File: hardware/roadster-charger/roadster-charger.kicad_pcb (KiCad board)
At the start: 4 copper layers, 74.4 x 50.2 mm, 98 parts, among them J1 USB4505-03-0-A, J2 USB4505-03-0-A, J3 54-00166, Q1 CSD19532Q5B, Q2 CSD19532Q5B, Q3 CSD19532Q5B, U1 MPM3606AGQV-P, U10 DAC70501ZDQFT, U11 LTC3786EUD#TRPBF, U2 ESP32-C3-MINI-1, U3 INA168, U4 OPA340NA, U5 FUSB307BMPX, U6 LM75B, U7 LM5050-1, U8 INA168, U9 OPA340NA

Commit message: change vout voltage divider to target max 2.5V @ 50V at battery
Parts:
- R18: value 15K -> 19.1K
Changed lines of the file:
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@@
     (descr "Resistor SMD 0603 (1608 Metric), square (rectangular) end terminal, IPC_7351 nominal, (Body size source: IPC-SM-782 page 72, https://www.pcb-3d.com/wordpress/wp-content/uploads/ipc-sm-782a_amendment_1_and_2.pdf), generated with kicad-footprint-generator")
     (tags "resistor")
-    (property "MPN" "RC0603JR-0715KL")
+    (property "MPN" "RMCF0603FT19K1")
     (property "Sheetfile" "roadster-charger.kicad_sch")
     (property "Sheetname" "")
@@
         (effects (font (size 1 1) (thickness 0.15)))
     )
-    (fp_text value "15K" (at 0 1.43 90) (layer "F.Fab") hide
+    (fp_text value "19.1K" (at 0 1.43 90) (layer "F.Fab") hide
         (effects (font (size 1 1) (thickness 0.15)))
     )

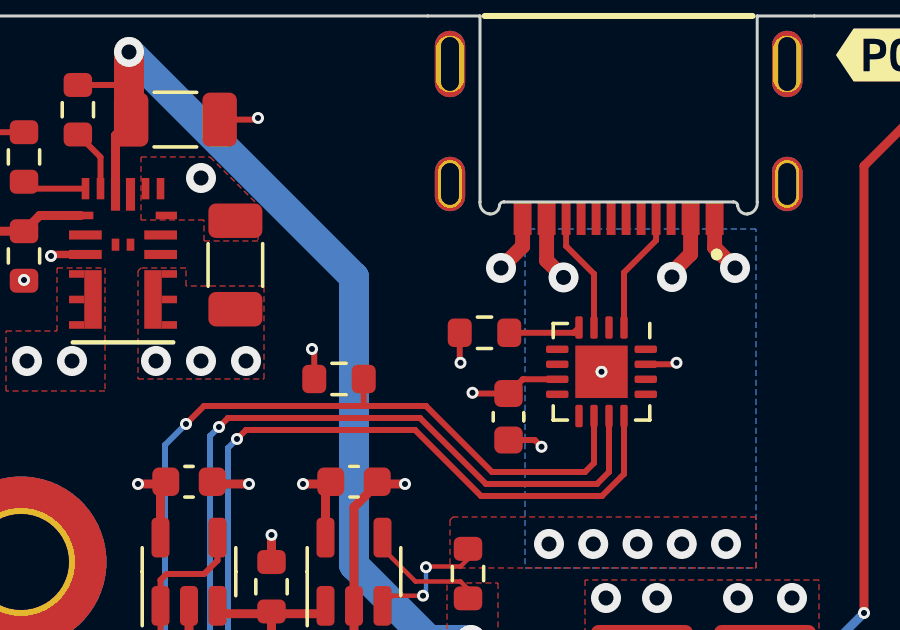
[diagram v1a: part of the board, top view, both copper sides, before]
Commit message: connect FUSB307 vbus pin
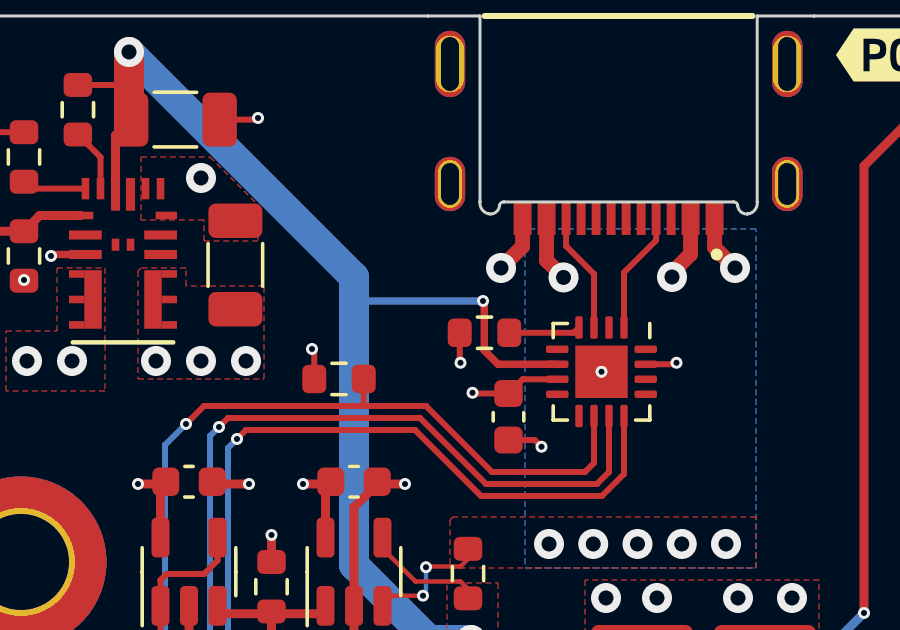
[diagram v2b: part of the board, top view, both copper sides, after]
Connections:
- U5 pad 6: unconnected-(U5-VBUS-Pad6) -> VBUS
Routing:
- net VBUS: track 62.2 -> 70.8 mm, vias 5 -> 6

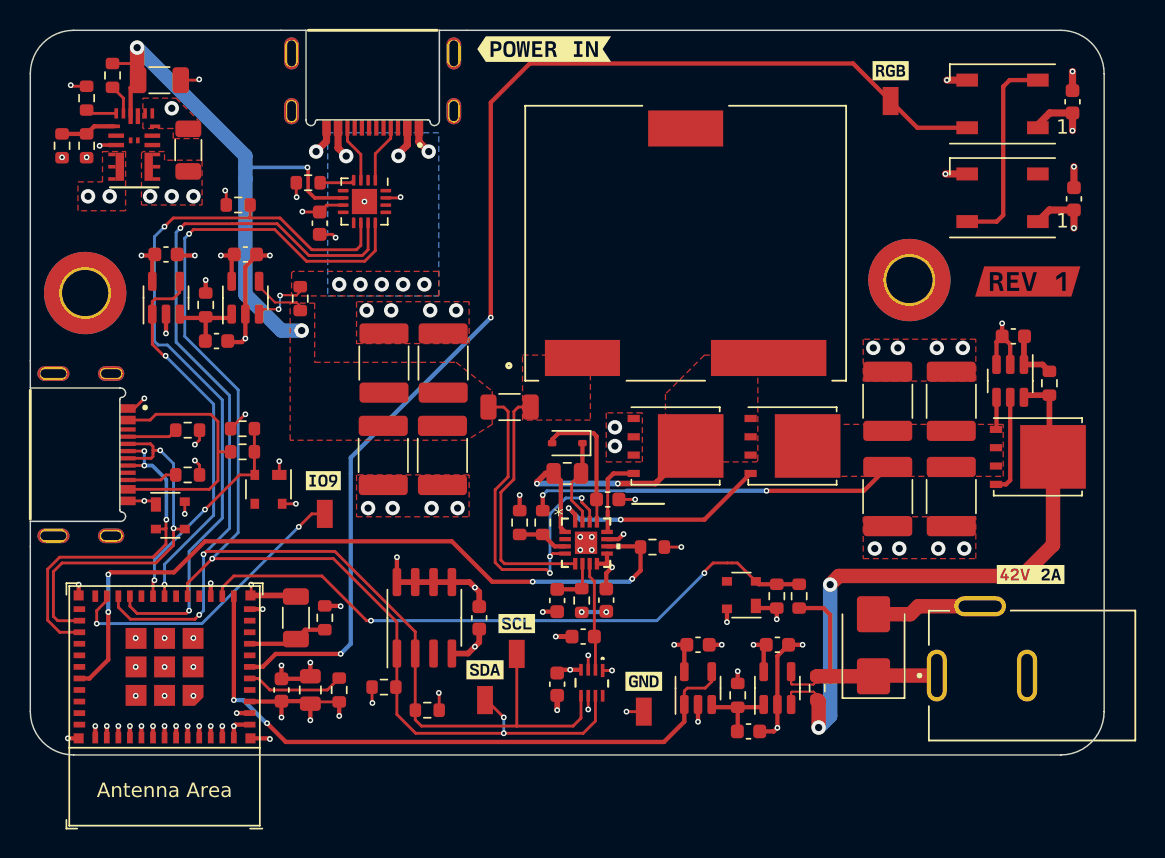
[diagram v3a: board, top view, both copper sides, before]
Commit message: Rough rev 2 layout
Move boost run pin to GPIO6 to avoid hard coded UART output
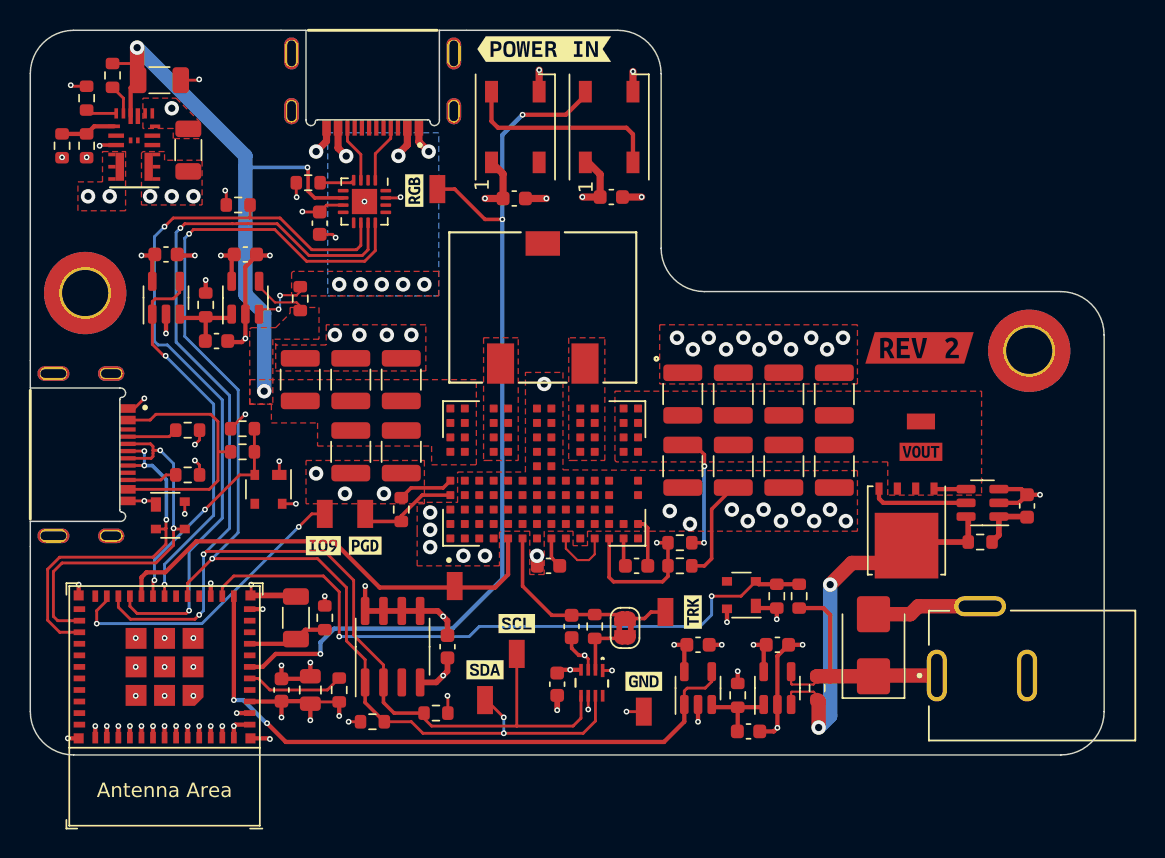
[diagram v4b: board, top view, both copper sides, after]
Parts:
- removed D7: D_Schottky_Small, Diode_SMD:D_SOD-323
- removed Q2, Q3: CSD19532Q5B, Package_TO_SOT_SMD:TDSON-8-1
- removed R22: 8.66K, Resistor_SMD:R_0603_1608Metric
- removed U11: LTC3786EUD#TRPBF, LTC3786EUD_TRPBF:QFN-16_UD
- removed kibuzzard-657BAFE4: G***, kibuzzard-657BAFE4
- removed kibuzzard-657BC539: G***, kibuzzard-657BC539
- removed kibuzzard-6581F29A: G***, kibuzzard-6581F29A
- removed kibuzzard-6581F2BF: G***, kibuzzard-6581F2BF
- added C31: 2.2uF, Capacitor_SMD:C_1210_3225Metric, F.Cu at (238.0, 139.5)
- added C32: 2.2uF, Capacitor_SMD:C_1210_3225Metric, F.Cu at (238.0, 134.5)
- added C33: 2.2uF, Capacitor_SMD:C_1210_3225Metric, F.Cu at (234.5, 134.5)
- added JP1: SolderJumper_2_Bridged, Jumper:SolderJumper-2_P1.3mm_Bridged2Bar_RoundedPad1.0x1.5mm, F.Cu at (223.5, 150.7)
- added TP6: RCU-0C, RCU-0C:TP+195X110, F.Cu at (205.5, 142.8)
- added TP7: RCU-0C, RCU-0C:TP+195X110, F.Cu at (211.7, 147.8)
- added TP8: RCU-0C, RCU-0C:TP+195X110, F.Cu at (226.3, 149.6)
- added TP9: RCU-0C, RCU-0C:TP+195X110, F.Cu at (244.0, 136.4)
- added U12: PI3740-00-LGIZ, PI3740-00-LGIZ:LGA108S100P10X14_1000X1400X263N, F.Cu at (217.9, 140.0)
- added kibuzzard-671EA982: G***, kibuzzard-671EA982, F.Cu at (205.5, 145.0)
- added kibuzzard-671EA992: G***, kibuzzard-671EA992, F.Cu at (228.2, 149.6)
- added kibuzzard-671EAE84: G***, kibuzzard-671EAE84, F.Cu at (208.9, 120.4)
- added kibuzzard-671EB1B0: G***, kibuzzard-671EB1B0, F.Cu at (243.9, 131.3)
- added kibuzzard-671EB361: G***, kibuzzard-671EB361, F.Cu at (244.0, 138.5)
- C19: value 15nF -> 56pF
- C20: value 220pF -> 4.7nF
- C21: value 0.1uF -> 2.2uF; footprint Capacitor_SMD:C_0805_2012Metric -> Capacitor_SMD:C_1210_3225Metric
- C22: value 4.7uF -> 2.2uF; footprint Capacitor_SMD:C_0603_1608Metric -> Capacitor_SMD:C_1210_3225Metric
- C23, C24, C25, C26, C27, C28, C29, C30: value 6.8uF -> 2.2uF; footprint Capacitor_SMD:C_1812_4532Metric -> Capacitor_SMD:C_1210_3225Metric
- L1: value 16uH -> PA5119.421NLT; footprint PA2050.193NL:IND_PA2050.193NL -> footprints:SMT_119.421NLT_PUL
- R23: value 8.66K -> 1K
- R24: value 8m -> 10K; footprint Resistor_SMD:R_1206_3216Metric -> Resistor_SMD:R_0603_1608Metric
- R25: value 475K -> 1K
- R26: value 12.1K -> 25K
- moved C10 38.8 mm to (215.8, 121.0), turned to 0 degrees
- moved D2 34.1 mm to (215.9, 116.0), turned to 90 degrees
- moved C26 33.8 mm to (208.0, 138.5)
- moved C11 32.6 mm to (222.6, 120.8), turned to 0 degrees
- moved TP2 32.0 mm to (210.5, 120.3), turned to -90 degrees
- moved D1 27.3 mm to (222.4, 116.0), turned to 90 degrees
- moved C30 20.8 mm to (227.5, 139.5)
- moved C28 20.2 mm to (231.0, 139.5)
- moved C22 19.6 mm to (204.5, 133.5), turned to 90 degrees
- moved C21 19.6 mm to (201.0, 133.5), turned to 90 degrees
- moved C24 18.6 mm to (227.5, 134.5)
- moved G*** 15.2 mm to (221.0, 137.6)
- moved R13 12.0 mm to (248.1, 144.8), turned to 0 degrees
- moved C27 11.8 mm to (234.5, 139.5)
- moved C13 11.8 mm to (251.3, 142.2), turned to 90 degrees
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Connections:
- C18 pad 1: Net-(U10-VOUT) -> Net-(JP1-B)
- C20 pad 1: /boost/ITH -> Net-(U12-COMP)
- C21 pad 1: Net-(Q2-D) -> VBUS
- C21 pad 2: Net-(D7-K) -> GND
- C22 pad 1: Net-(D7-A) -> VBUS
- C26 pad 1: /boost/BOOST_VOUT -> VBUS
- C28 pad 1: VBUS -> /boost/BOOST_VOUT
- C30 pad 1: VBUS -> /boost/BOOST_VOUT
- L1 pad 1: Net-(U11-SENSE-) -> Net-(L1-Pad1)
- L1 pad 2: Net-(Q2-D) -> Net-(L1-Pad2)
- R23 pad 1: /BOOST_RUN -> Net-(U12-EAIN)
- R24 pad 1: VBUS -> Net-(U12-VDR)
- R24 pad 2: Net-(U11-SENSE-) -> Net-(U12-PGD)
- R25 pad 1: /boost/BOOST_VOUT -> Net-(JP1-B)
- R25 pad 2: /boost/VFB -> Net-(JP1-A)
- R26 pad 1: /boost/VFB -> /boost/BOOST_VOUT
- R26 pad 2: GND -> Net-(U12-EAIN)
- U10 pad 2: Net-(U10-VOUT) -> Net-(JP1-A)
- U2 pad 20: unconnected-(U2-GPIO6-Pad20) -> /BOOST_RUN
- U2 pad 31: /BOOST_RUN -> unconnected-(U2-GPIO21/U0TXD-Pad31)
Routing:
- net VBUS: track 70.8 -> 46.9 mm, vias 6 -> 3
- net /RGB_DATA: track 85.1 -> 63.8 mm, vias 2 -> 3
- net /BOOST_RUN: track 51.7 -> 31.9 mm, vias 4 -> 0
- net Net-(Q2-D): track 17.7 -> 0.00 mm, vias 2 -> 0
- net Net-(U11-SENSE-): track 17.2 -> 0.00 mm
- net /boost/BOOST_VOUT: track 28.0 -> 11.0 mm
- net Net-(Q1-D): track 44.2 -> 27.9 mm
- net Net-(Q3-G): track 15.4 -> 0.00 mm, vias 2 -> 0
- net Net-(JP1-B): track 0.00 -> 14.4 mm
- net Net-(U12-EAIN): track 0.00 -> 10.2 mm, vias 0 -> 1
- net Net-(D7-A): track 9.54 -> 0.00 mm
- net Net-(U10-VOUT): track 7.51 -> 0.00 mm
- net Net-(U12-PGD): track 0.00 -> 6.85 mm
- net Net-(D7-K): track 6.21 -> 0.00 mm
- net Net-(Q2-G): track 5.64 -> 0.00 mm
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- added copper zone on F.Cu, net Net-(L1-Pad1)
- added copper zone on F.Cu, net Net-(L1-Pad2)
- removed copper zone on F.Cu, net Net-(Q2-D)
- removed copper zone on F.Cu, net Net-(U11-SENSE-)
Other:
- outline, holes or cut-outs redrawn

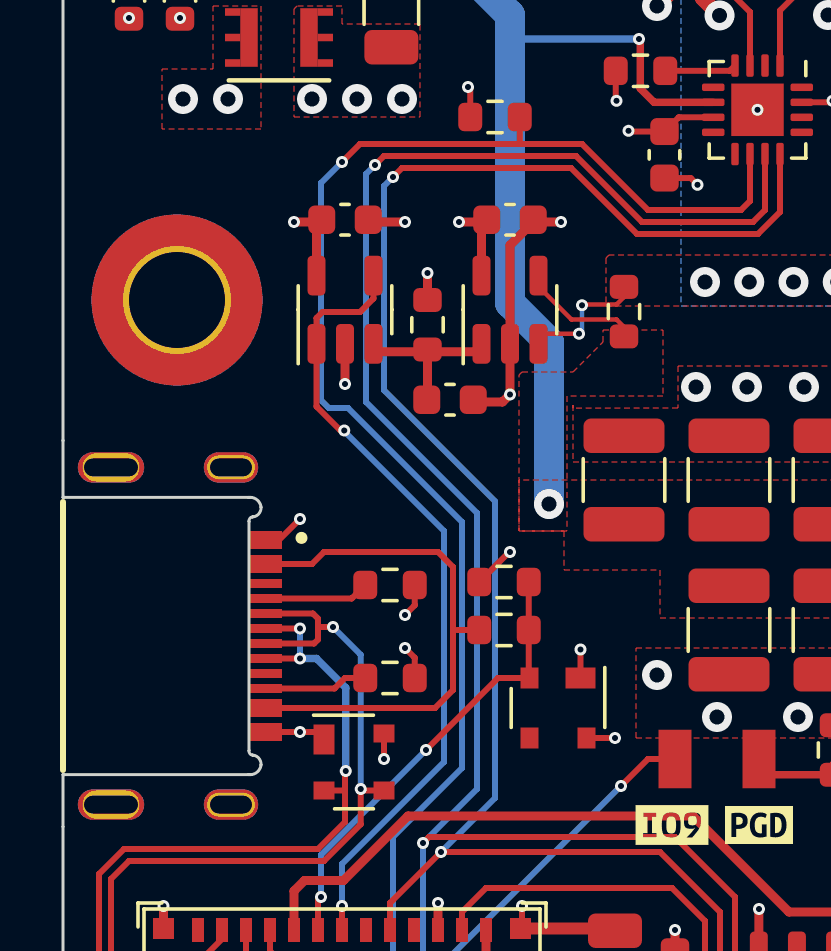
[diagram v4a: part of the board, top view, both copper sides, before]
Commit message: add debug connected LED
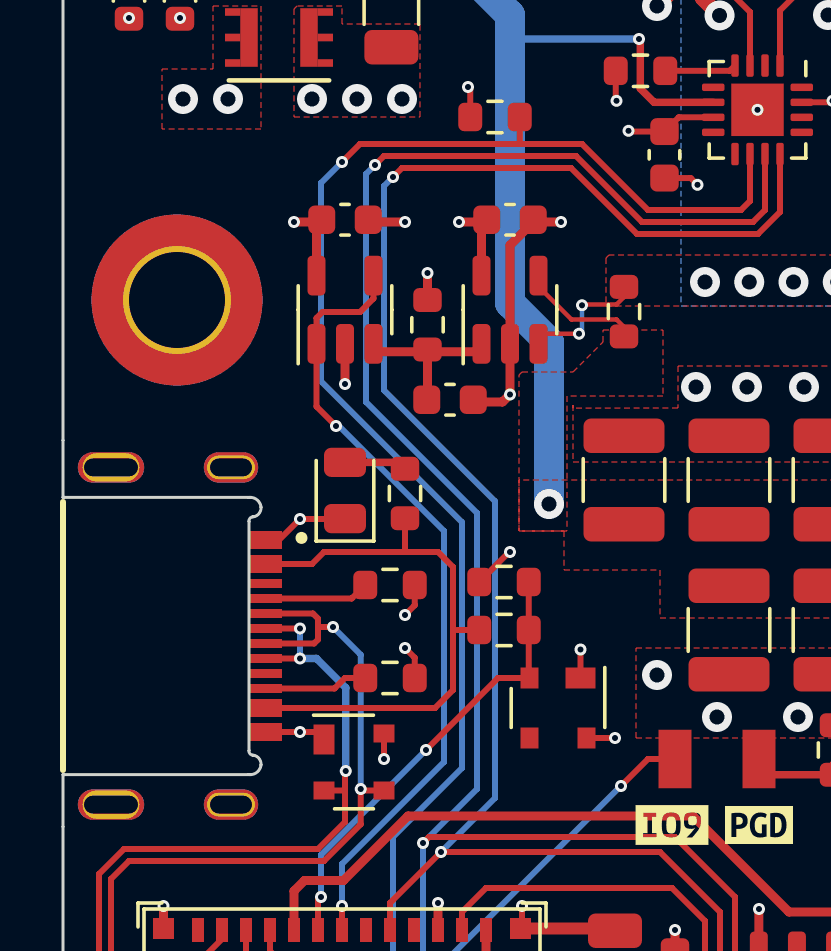
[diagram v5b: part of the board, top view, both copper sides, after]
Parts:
- added D7: Green, LED_SMD:LED_0805_2012Metric, F.Cu at (191.7, 133.8)
- added R22: 300, Resistor_SMD:R_0603_1608Metric, F.Cu at (193.7, 133.9)
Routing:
- net Net-(D7-A): track 0.00 -> 2.09 mm
- net GND: track 108.5 -> 110.0 mm
- net /DBG_VBUS: track 18.0 -> 19.1 mm

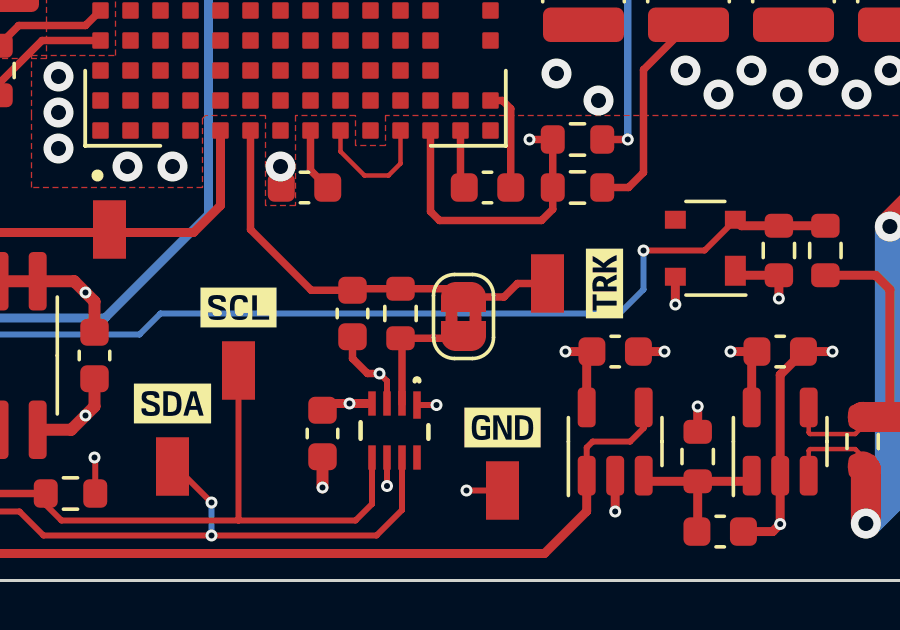
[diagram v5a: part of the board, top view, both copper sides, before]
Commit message: change all 1K Rs to 0.1%, invert DAC jumpers
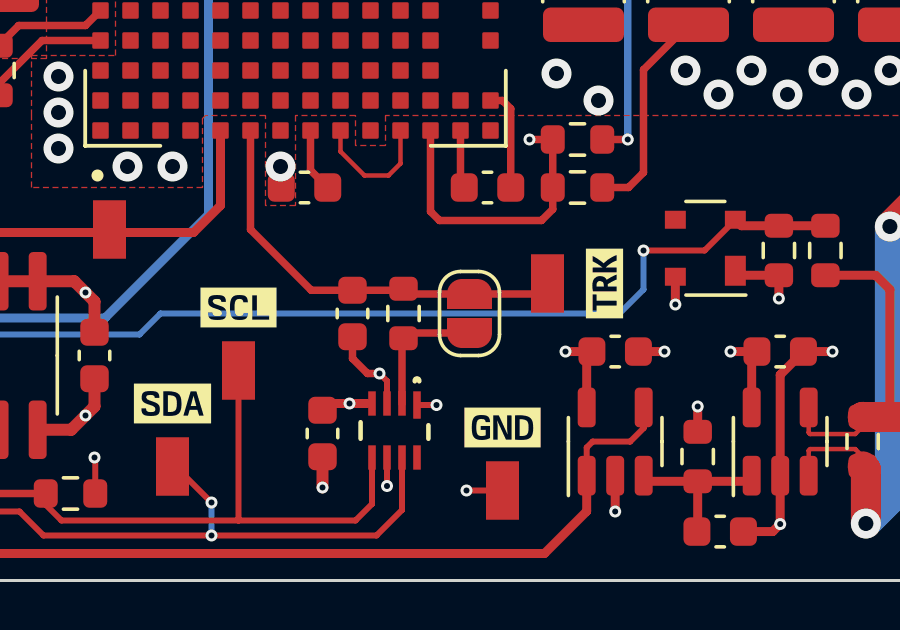
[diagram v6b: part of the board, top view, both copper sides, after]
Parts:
- JP1: value SolderJumper_2_Bridged -> SolderJumper_2_Open; footprint Jumper:SolderJumper-2_P1.3mm_Bridged2Bar_RoundedPad1.0x1.5mm -> Jumper:SolderJumper-2_P1.3mm_Open_RoundedPad1.0x1.5mm
- moved JP1 0.22 mm to (223.7, 150.6), turned to -90 degrees
- moved R25 0.10 mm to (221.5, 150.6), turned to 90 degrees
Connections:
- C18 pad 1: Net-(JP1-B) -> Net-(JP1-A)
- TP8 pad 1: Net-(JP1-B) -> Net-(JP1-A)
- U10 pad 2: Net-(JP1-A) -> Net-(JP1-B)
- U12 pad A6: Net-(JP1-B) -> Net-(JP1-A)
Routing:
- net Net-(JP1-A): track 4.33 -> 14.3 mm
- net Net-(JP1-B): track 14.4 -> 4.47 mm
